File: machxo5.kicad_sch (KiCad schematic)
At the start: 63 parts, among them J2 PinHeader_2x5_P1.27mm_SMD, J3 PinHeader_2x5_P1.27mm_SMD, SW1 SW_KSC441J70SHLFS_SMD, SW2 SW_KSC441J70SHLFS_SMD, U1 LFMXO5-25-7BBG400C, Y1 Oscillator_125MHz_ASEMB

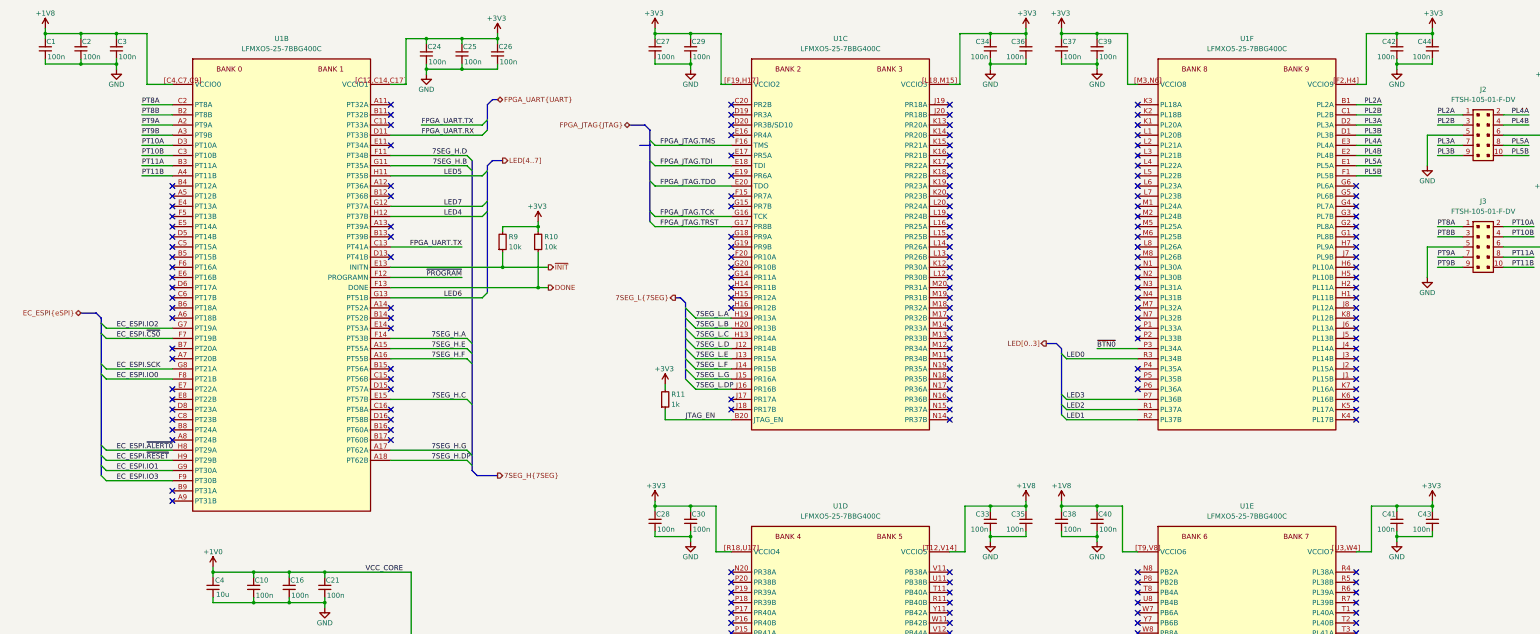
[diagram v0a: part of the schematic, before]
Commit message: [#103953] Sch: Update DCDC
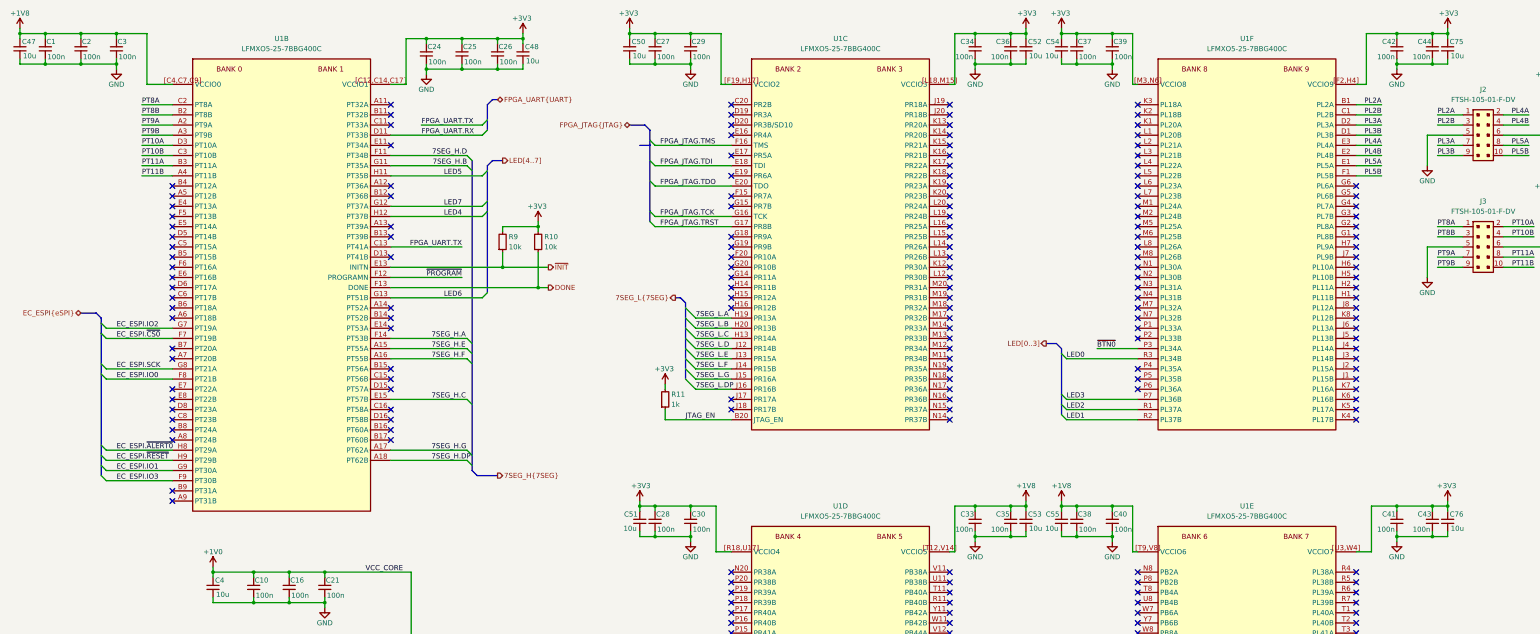
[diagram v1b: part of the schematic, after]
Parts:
- added C47, C48, C50, C51, C52, C53, C54, C55, C75, C76: C_10u_6.3V_0402, antmicro-footprints:C_0402_1005Metric, symbol antmicroCapacitors0402:C_10u_6.3V_0402
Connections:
- net +1V8: now also C47.2, C53.2, C55.2
- net +3V3: now also C48.2, C50.2, C51.2, C52.2, C54.2, C75.2, C76.2
- net GND: now also C47.1, C48.1, C50.1, C51.1, C52.1, C53.1, C54.1, C55.1, C75.1, C76.1
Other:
- moved on the sheet: C33, C34, C35, C36, C37, C38, C39, C40
